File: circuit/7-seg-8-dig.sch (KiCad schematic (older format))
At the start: 5 parts, among them U1 CC56-12EWA, U2 MAX7219, U3 CC56-12EWA

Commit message: Updated display footprint
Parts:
- U1, U3: footprint Display_7Segment:CA56-12EWA -> circuit:7seg
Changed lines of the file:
@@
 F 0 "U53" H 3450 3067 50  0000 C CNN
 F 1 "CC56-12EWA" H 3450 2976 50  0000 C CNN
-F 2 "Display_7Segment:CA56-12EWA" H 3450 1800 50  0001 C CNN
+F 2 "circuit:7seg" H 3450 1800 50  0001 C CNN
 F 3 "http://www.kingbrightusa.com/images/catalog/SPEC/CA56-12EWA.pdf" H 3020 2430 50  0001 C CNN
 	1    3450 2400
@@
 F 0 "U55" H 6200 3067 50  0000 C CNN
 F 1 "CC56-12EWA" H 6200 2976 50  0000 C CNN
-F 2 "Display_7Segment:CA56-12EWA" H 6200 1800 50  0001 C CNN
+F 2 "circuit:7seg" H 6200 1800 50  0001 C CNN
 F 3 "http://www.kingbrightusa.com/images/catalog/SPEC/CA56-12EWA.pdf" H 5770 2430 50  0001 C CNN
 	1    6200 2400

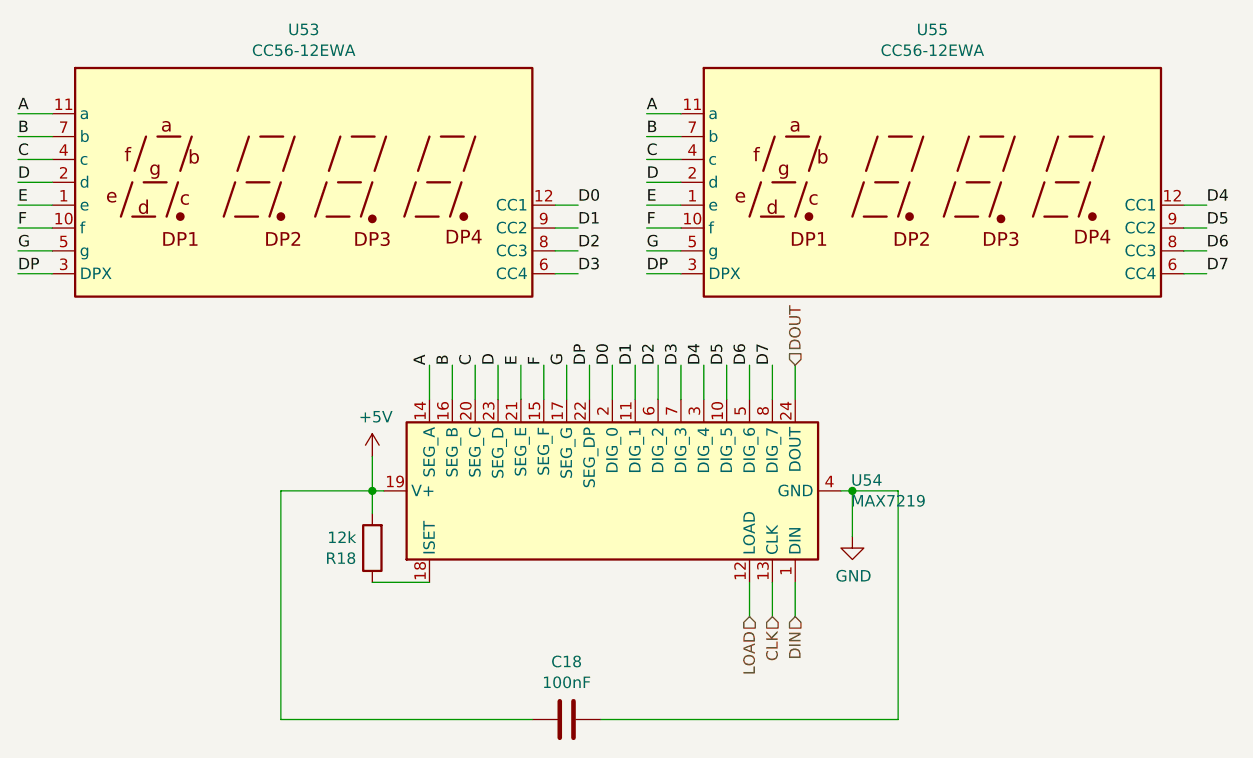
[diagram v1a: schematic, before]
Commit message: Added microcontroller circuit
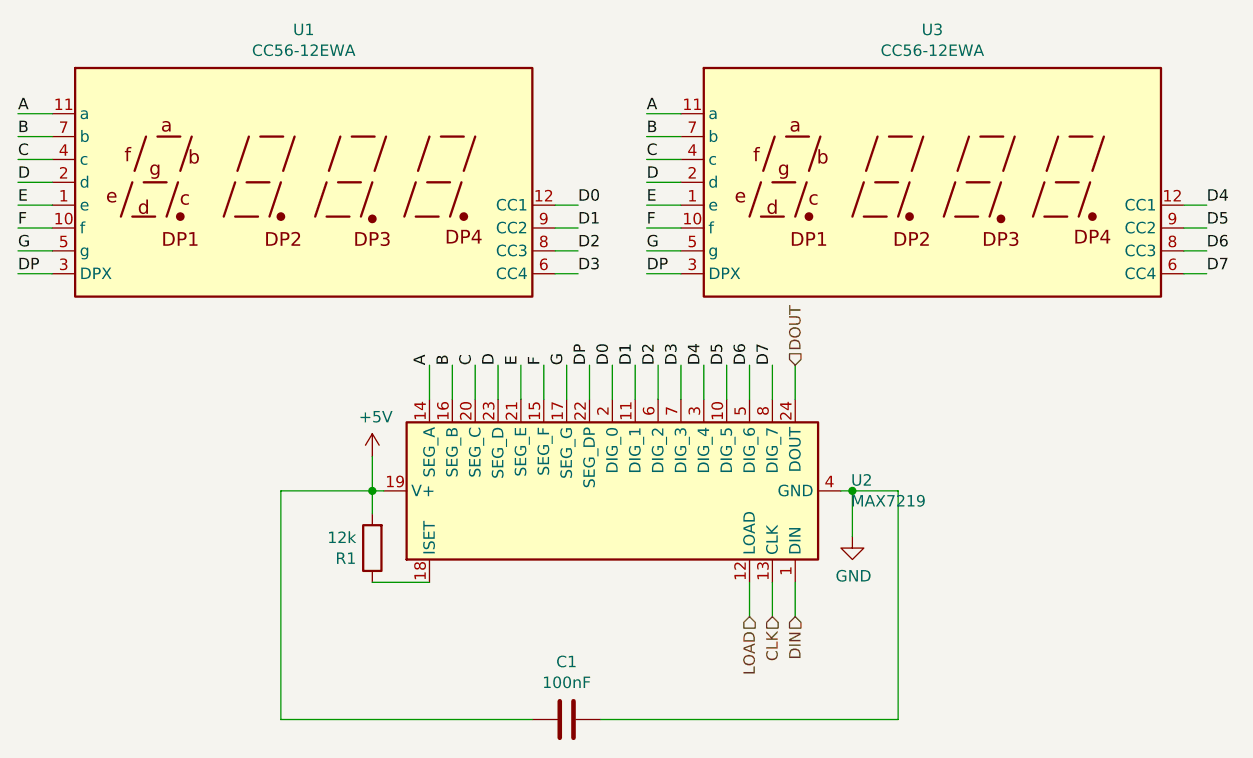
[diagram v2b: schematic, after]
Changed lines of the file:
@@
 $Descr A4 11693 8268
 encoding utf-8
-Sheet 21 21
+Sheet 2 21
 Title ""
 Date ""
@@
 AR Path="/5E35D21E/5E380CD7" Ref="U50"  Part="1"
 AR Path="/5E35D4DB/5E380CD7" Ref="U53"  Part="1"
-F 0 "U53" H 3450 3067 50  0000 C CNN
+F 0 "U1" H 3450 3067 50  0000 C CNN
 F 1 "CC56-12EWA" H 3450 2976 50  0000 C CNN
 F 2 "circuit:7seg" H 3450 1800 50  0001 C CNN
@@
 AR Path="/5E35D21E/5E380CDD" Ref="U51"  Part="1"
 AR Path="/5E35D4DB/5E380CDD" Ref="U54"  Part="1"
-F 0 "U54" V 4846 2706 50  0000 R CNN
+F 0 "U2" V 4846 2706 50  0000 R CNN
 F 1 "MAX7219" V 4755 2706 50  0000 R CNN
 F 2 "Package_SO:SOIC-24W_7.5x15.4mm_P1.27mm" H 4750 3800 50  0001 C CNN
@@
 AR Path="/5E35D21E/5E380CE3" Ref="U52"  Part="1"
 AR Path="/5E35D4DB/5E380CE3" Ref="U55"  Part="1"
-F 0 "U55" H 6200 3067 50  0000 C CNN
+F 0 "U3" H 6200 3067 50  0000 C CNN
 F 1 "CC56-12EWA" H 6200 2976 50  0000 C CNN
 F 2 "circuit:7seg" H 6200 1800 50  0001 C CNN
@@
 AR Path="/5E35D21E/5E388E6B" Ref="R17"  Part="1"
 AR Path="/5E35D4DB/5E388E6B" Ref="R18"  Part="1"
-F 0 "R18" H 3820 4046 50  0000 L CNN
+F 0 "R1" H 3820 4046 50  0000 L CNN
 F 1 "12k" H 3820 3955 50  0000 L CNN
 F 2 "Resistor_SMD:R_0805_2012Metric_Pad1.15x1.40mm_HandSolder" V 3680 4000 50  0001 C CNN
@@
 AR Path="/5E35D21E/5E38E534" Ref="C17"  Part="1"
 AR Path="/5E35D4DB/5E38E534" Ref="C18"  Part="1"
-F 0 "C18" V 4348 4750 50  0000 C CNN
+F 0 "C1" V 4348 4750 50  0000 C CNN
 F 1 "100nF" V 4439 4750 50  0000 C CNN
 F 2 "Capacitor_SMD:C_0805_2012Metric_Pad1.15x1.40mm_HandSolder" H 4638 4600 50  0001 C CNN
